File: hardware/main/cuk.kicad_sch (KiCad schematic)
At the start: 54 parts, among them Q401 BSC093N15NS5, Q402 BSC093N15NS5

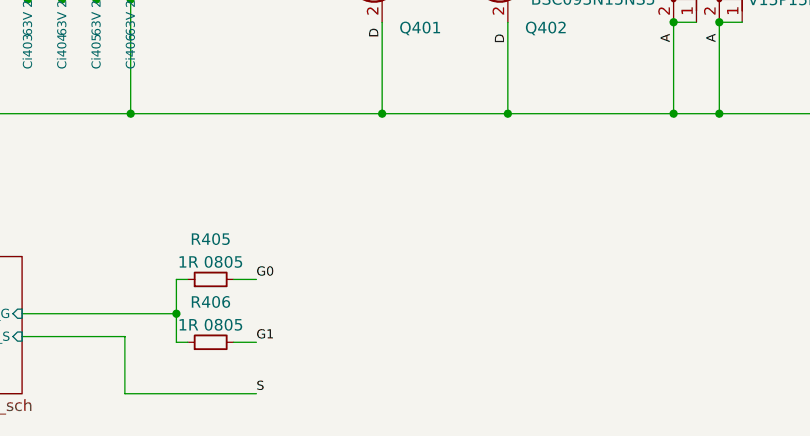
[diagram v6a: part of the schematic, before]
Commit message: Layout: Fist version of power stage
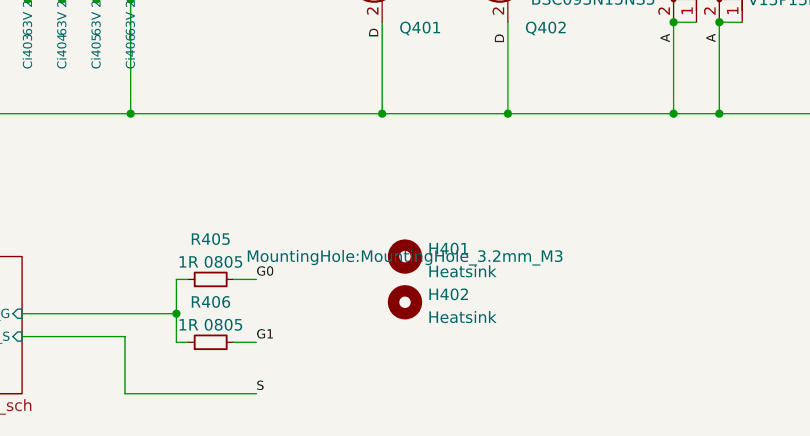
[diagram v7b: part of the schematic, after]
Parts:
- added H401, H402: Heatsink, MountingHole:MountingHole_3.2mm_M3, symbol Mechanical:MountingHole
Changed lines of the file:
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@@
     (pin "2")
+  )
+  (symbol (lib_id "Mechanical:MountingHole") (at 129.54 147.32 0) (unit 1)
+    (in_bom yes) (on_board yes) (fields_autoplaced)
+    (property "Reference" "H401" (id 0) (at 132.08 146.4853 0)
+      (effects (font (size 1.27 1.27)) (justify left))
+    )
+    (property "Value" "Heatsink" (id 1) (at 132.08 149.0222 0)
+      (effects (font (size 1.27 1.27)) (justify left))
+    )
+    (property "Footprint" "MountingHole:MountingHole_3.2mm_M3" (id 2) (at 129.54 147.32 0))
+    (property "Datasheet" "~" (id 3) (at 129.54 147.32 0)
+      (effects (font (size 1.27 1.27)) hide)
+    )
   )
   (symbol (lib_id "Device:C_Small") (at 149.225 90.805 270) (unit 1)
@@
     (pin "2")
   )
+  (symbol (lib_id "Mechanical:MountingHole") (at 129.54 152.4 0) (unit 1)
+    (in_bom yes) (on_board yes) (fields_autoplaced)
+    (property "Reference" "H402" (id 0) (at 132.08 151.5653 0)
+      (effects (font (size 1.27 1.27)) (justify left))
+    )
+    (property "Value" "Heatsink" (id 1) (at 132.08 154.1022 0)
+      (effects (font (size 1.27 1.27)) (justify left))
+    )
+    (property "Footprint" "MountingHole:MountingHole_3.2mm_M3" (id 2) (at 129.54 152.4 0)
+      (effects (font (size 1.27 1.27)) hide)
+    )
+    (property "Datasheet" "~" (id 3) (at 129.54 152.4 0)
+      (effects (font (size 1.27 1.27)) hide)
+    )
+  )
   (symbol (lib_id "Device:Q_NMOS_GDS") (at 138.43 116.205 0) (mirror x) (unit 1)

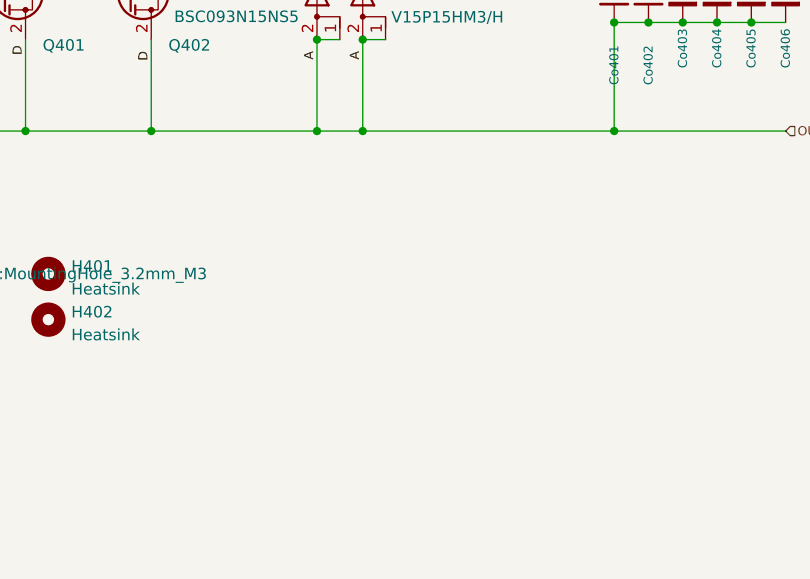
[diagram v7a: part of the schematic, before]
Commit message: Layout: Organize and initialize routing of control
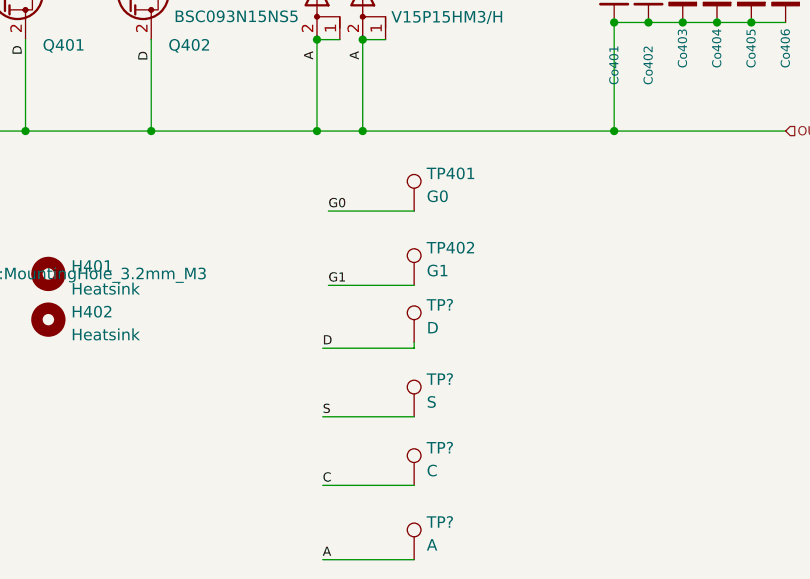
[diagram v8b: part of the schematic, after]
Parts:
- added TP401: G0, TestPoint:TestPoint_Pad_1.5x1.5mm, symbol Connector:TestPoint
- added TP402: G1, TestPoint:TestPoint_Pad_1.5x1.5mm, symbol Connector:TestPoint
- added TP?: A, TestPoint:TestPoint_Pad_1.5x1.5mm, symbol Connector:TestPoint
- added TP?: S, TestPoint:TestPoint_Pad_1.5x1.5mm, symbol Connector:TestPoint
- added TP?: C, TestPoint:TestPoint_Pad_1.5x1.5mm, symbol Connector:TestPoint
- added TP?: D, TestPoint:TestPoint_Pad_1.5x1.5mm, symbol Connector:TestPoint
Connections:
- net C: now also TP?.1
- net G0: now also TP401.1
- net G1: now also TP402.1
- net IN+: now also TP?.1, TP?.1
- net S: now also TP?.1
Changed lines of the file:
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@@
+    (stroke (width 0) (type default) (color 0 0 0 0))
+  )
+  (wire (pts (xy 170.18 155.575) (xy 170.18 154.94))
     (stroke (width 0) (type default) (color 0 0 0 0))
   )
@@
     (stroke (width 0) (type default) (color 0 0 0 0))
   )
+  (wire (pts (xy 160.655 148.59) (xy 170.18 148.59))
+    (stroke (width 0) (type default) (color 0 0 0 0))
+  )
   (wire (pts (xy 196.215 114.3) (xy 200.025 114.3))
     (stroke (width 0) (type default) (color 0 0 0 0))
@@
     (stroke (width 0) (type default) (color 0 0 0 0))
   )
+  (wire (pts (xy 160.02 155.575) (xy 170.18 155.575))
+    (stroke (width 0) (type default) (color 0 0 0 0))
+  )
   (wire (pts (xy 66.04 34.29) (xy 66.04 31.115))
     (stroke (width 0) (type default) (color 0 0 0 0))
   )
+  (wire (pts (xy 160.02 163.195) (xy 170.18 163.195))
+    (stroke (width 0) (type default) (color 0 0 0 0))
+  )
   (wire (pts (xy 146.685 78.105) (xy 146.685 81.28))
     (stroke (width 0) (type default) (color 0 0 0 0))
@@
     (stroke (width 0) (type default) (color 0 0 0 0))
   )
+  (wire (pts (xy 160.02 170.815) (xy 170.18 170.815))
+    (stroke (width 0) (type default) (color 0 0 0 0))
+  )
   (wire (pts (xy 151.765 97.155) (xy 151.765 100.33))
     (stroke (width 0) (type default) (color 0 0 0 0))
@@
     (stroke (width 0) (type default) (color 0 0 0 0))
   )
+  (wire (pts (xy 160.655 140.335) (xy 170.18 140.335))
+    (stroke (width 0) (type default) (color 0 0 0 0))
+  )
   (wire (pts (xy 67.945 34.29) (xy 66.04 34.29))
     (stroke (width 0) (type default) (color 0 0 0 0))
@@
     (stroke (width 0) (type default) (color 0 0 0 0))
   )
+  (wire (pts (xy 160.02 179.07) (xy 170.18 179.07))
+    (stroke (width 0) (type default) (color 0 0 0 0))
+  )
   (wire (pts (xy 169.545 41.275) (xy 173.355 41.275))
     (stroke (width 0) (type default) (color 0 0 0 0))
@@
   )
   (text "Snubber Mosfet" (at 185.42 58.42 0)
+    (effects (font (size 1.016 1.016)) (justify left bottom))
+  )
+  (label "D" (at 160.02 155.575 0)
     (effects (font (size 1.016 1.016)) (justify left bottom))
   )
@@
     (effects (font (size 1.016 1.016)) (justify right bottom))
   )
+  (label "S" (at 160.02 163.195 0)
+    (effects (font (size 1.016 1.016)) (justify left bottom))
+  )
+  (label "C" (at 160.02 170.815 0)
+    (effects (font (size 1.016 1.016)) (justify left bottom))
+  )
+  (label "G0" (at 160.655 140.335 0)
+    (effects (font (size 1.016 1.016)) (justify left bottom))
+  )
   (label "S" (at 66.04 54.61 90)
     (effects (font (size 1.016 1.016)) (justify left bottom))
@@
     (effects (font (size 1.016 1.016)) (justify right bottom))
   )
+  (label "A" (at 160.02 179.07 0)
+    (effects (font (size 1.016 1.016)) (justify left bottom))
+  )
   (label "A" (at 215.265 54.61 180)
     (effects (font (size 1.016 1.016)) (justify right bottom))
@@
     (effects (font (size 1.016 1.016)) (justify left bottom))
   )
+  (label "G1" (at 160.655 148.59 0)
+    (effects (font (size 1.016 1.016)) (justify left bottom))
+  )
   (label "S" (at 194.945 41.275 180)
     (effects (font (size 1.016 1.016)) (justify right bottom))
@@
     (pin "2")
   )
+  (symbol (lib_id "Connector:TestPoint") (at 170.18 179.07 0) (unit 1)
+    (in_bom yes) (on_board yes) (fields_autoplaced)
+    (property "Reference" "TP?" (id 0) (at 171.577 174.9333 0)
+      (effects (font (size 1.27 1.27)) (justify left))
+    )
+    (property "Value" "A" (id 1) (at 171.577 177.4702 0)
+      (effects (font (size 1.27 1.27)) (justify left))
+    )
+    (property "Footprint" "TestPoint:TestPoint_Pad_1.5x1.5mm" (id 2) (at 175.26 179.07 0)
+      (effects (font (size 1.27 1.27)) hide)
+    )
+    (property "Datasheet" "~" (id 3) (at 175.26 179.07 0)
+      (effects (font (size 1.27 1.27)) hide)
+    )
+    (pin "1")
+  )
   (symbol (lib_id "Device:R_Small") (at 64.135 46.355 180) (unit 1)
     (in_bom yes) (on_board yes)
@@
     (pin "1")
     (pin "2")
+  )
+  (symbol (lib_id "Connector:TestPoint") (at 170.18 148.59 0) (unit 1)
+    (in_bom yes) (on_board yes) (fields_autoplaced)
+    (property "Reference" "TP402" (id 0) (at 171.577 144.4533 0)
+      (effects (font (size 1.27 1.27)) (justify left))
+    )
+    (property "Value" "G1" (id 1) (at 171.577 146.9902 0)
+      (effects (font (size 1.27 1.27)) (justify left))
+    )
+    (property "Footprint" "TestPoint:TestPoint_Pad_1.5x1.5mm" (id 2) (at 175.26 148.59 0)
+      (effects (font (size 1.27 1.27)) hide)
+    )
+    (property "Datasheet" "~" (id 3) (at 175.26 148.59 0)
+      (effects (font (size 1.27 1.27)) hide)
+    )
+    (pin "1")
   )
   (symbol (lib_id "Device:C_Polarized_Small") (at 87.63 116.205 0) (mirror x) (unit 1)
@@
     (pin "1")
     (pin "2")
+  )
+  (symbol (lib_id "Connector:TestPoint") (at 170.18 140.335 0) (unit 1)
+    (in_bom yes) (on_board yes) (fields_autoplaced)
+    (property "Reference" "TP401" (id 0) (at 171.577 136.1983 0)
+      (effects (font (size 1.27 1.27)) (justify left))
+    )
+    (property "Value" "G0" (id 1) (at 171.577 138.7352 0)
+      (effects (font (size 1.27 1.27)) (justify left))
+    )
+    (property "Footprint" "TestPoint:TestPoint_Pad_1.5x1.5mm" (id 2) (at 175.26 140.335 0)
+      (effects (font (size 1.27 1.27)) hide)
+    )
+    (property "Datasheet" "~" (id 3) (at 175.26 140.335 0)
+      (effects (font (size 1.27 1.27)) hide)
+    )
+    (pin "1")
   )
   (symbol (lib_id "Device:C_Small") (at 173.355 36.83 180) (unit 1)
@@
     (pin "2")
   )
+  (symbol (lib_id "Connector:TestPoint") (at 170.18 163.195 0) (unit 1)
+    (in_bom yes) (on_board yes) (fields_autoplaced)
+    (property "Reference" "TP?" (id 0) (at 171.577 159.0583 0)
+      (effects (font (size 1.27 1.27)) (justify left))
+    )
+    (property "Value" "S" (id 1) (at 171.577 161.5952 0)
+      (effects (font (size 1.27 1.27)) (justify left))
+    )
+    (property "Footprint" "TestPoint:TestPoint_Pad_1.5x1.5mm" (id 2) (at 175.26 163.195 0)
+      (effects (font (size 1.27 1.27)) hide)
+    )
+    (property "Datasheet" "~" (id 3) (at 175.26 163.195 0)
+      (effects (font (size 1.27 1.27)) hide)
+    )
+    (pin "1")
+  )
   (symbol (lib_id "Device:R_Small") (at 107.95 156.845 90) (unit 1)
     (in_bom yes) (on_board yes) (fields_autoplaced)
@@
     (pin "2")
   )
+  (symbol (lib_id "Connector:TestPoint") (at 170.18 170.815 0) (unit 1)
+    (in_bom yes) (on_board yes) (fields_autoplaced)
+    (property "Reference" "TP?" (id 0) (at 171.577 166.6783 0)
+      (effects (font (size 1.27 1.27)) (justify left))
+    )
+    (property "Value" "C" (id 1) (at 171.577 169.2152 0)
+      (effects (font (size 1.27 1.27)) (justify left))
+    )
+    (property "Footprint" "TestPoint:TestPoint_Pad_1.5x1.5mm" (id 2) (at 175.26 170.815 0)
+      (effects (font (size 1.27 1.27)) hide)
+    )
+    (property "Datasheet" "~" (id 3) (at 175.26 170.815 0)
+      (effects (font (size 1.27 1.27)) hide)
+    )
+    (pin "1")
+  )
   (symbol (lib_id "Device:R_Small") (at 109.22 36.195 0) (unit 1)
     (in_bom yes) (on_board yes)
@@
     (pin "2")
   )
+  (symbol (lib_id "Connector:TestPoint") (at 170.18 154.94 0) (unit 1)
+    (in_bom yes) (on_board yes) (fields_autoplaced)
+    (property "Reference" "TP?" (id 0) (at 171.577 150.8033 0)
+      (effects (font (size 1.27 1.27)) (justify left))
+    )
+    (property "Value" "D" (id 1) (at 171.577 153.3402 0)
+      (effects (font (size 1.27 1.27)) (justify left))
+    )
+    (property "Footprint" "TestPoint:TestPoint_Pad_1.5x1.5mm" (id 2) (at 175.26 154.94 0)
+      (effects (font (size 1.27 1.27)) hide)
+    )
+    (property "Datasheet" "~" (id 3) (at 175.26 154.94 0)
+      (effects (font (size 1.27 1.27)) hide)
+    )
+    (pin "1")
+  )
   (symbol (lib_id "Device:C_Small") (at 149.225 87.63 270) (unit 1)
